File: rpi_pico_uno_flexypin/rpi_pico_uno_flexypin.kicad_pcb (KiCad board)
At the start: 2 copper layers, 68.6 x 53.3 mm, 118 parts, among them J1 Conn_01x20, J2 Conn_01x03, J3 Conn_01x20, J4 Conn_01x03, J5 Conn_SPI, J6 Conn_01x08, J7 Conn_01x06, J8 Conn_01x10, J9 Conn_01x08, SW1 SW_RST, U1 RaspberryPi_Pico

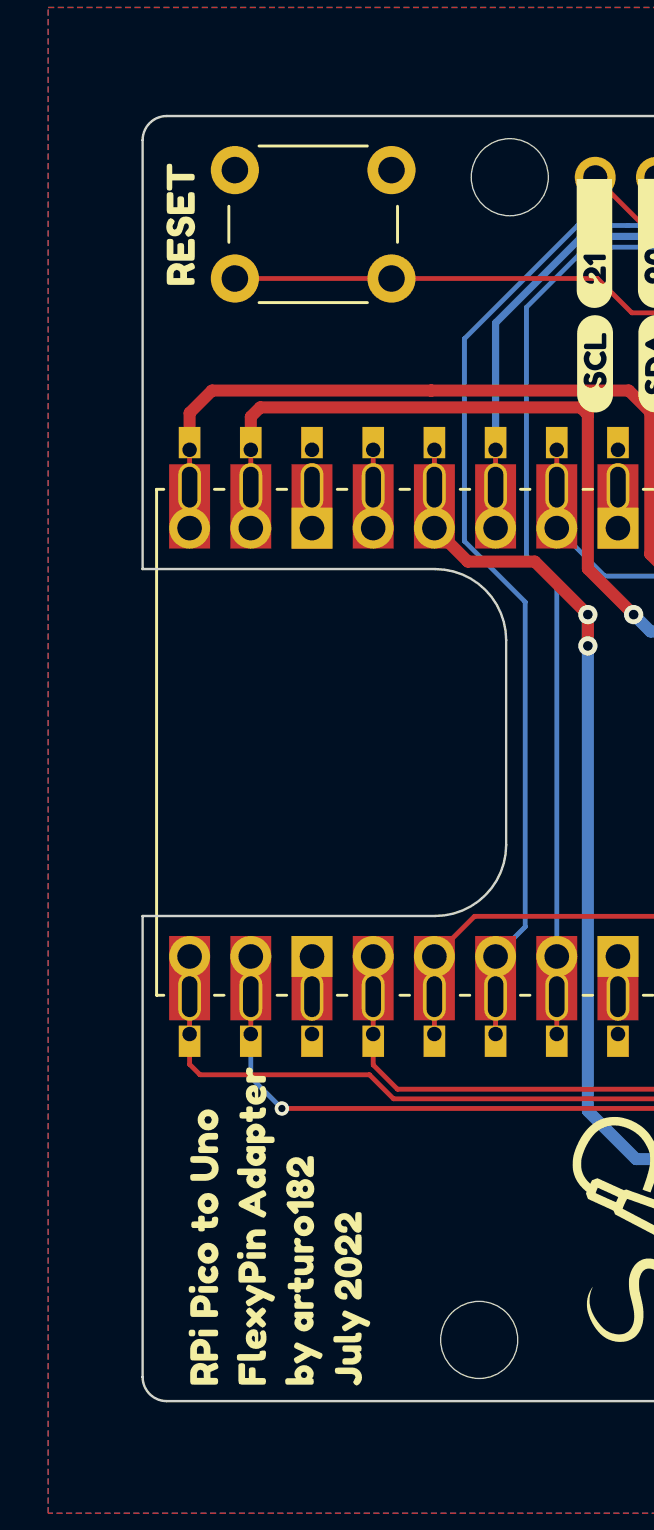
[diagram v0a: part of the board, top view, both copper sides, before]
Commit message: Change Pico Adapters' Reset Button to SMD
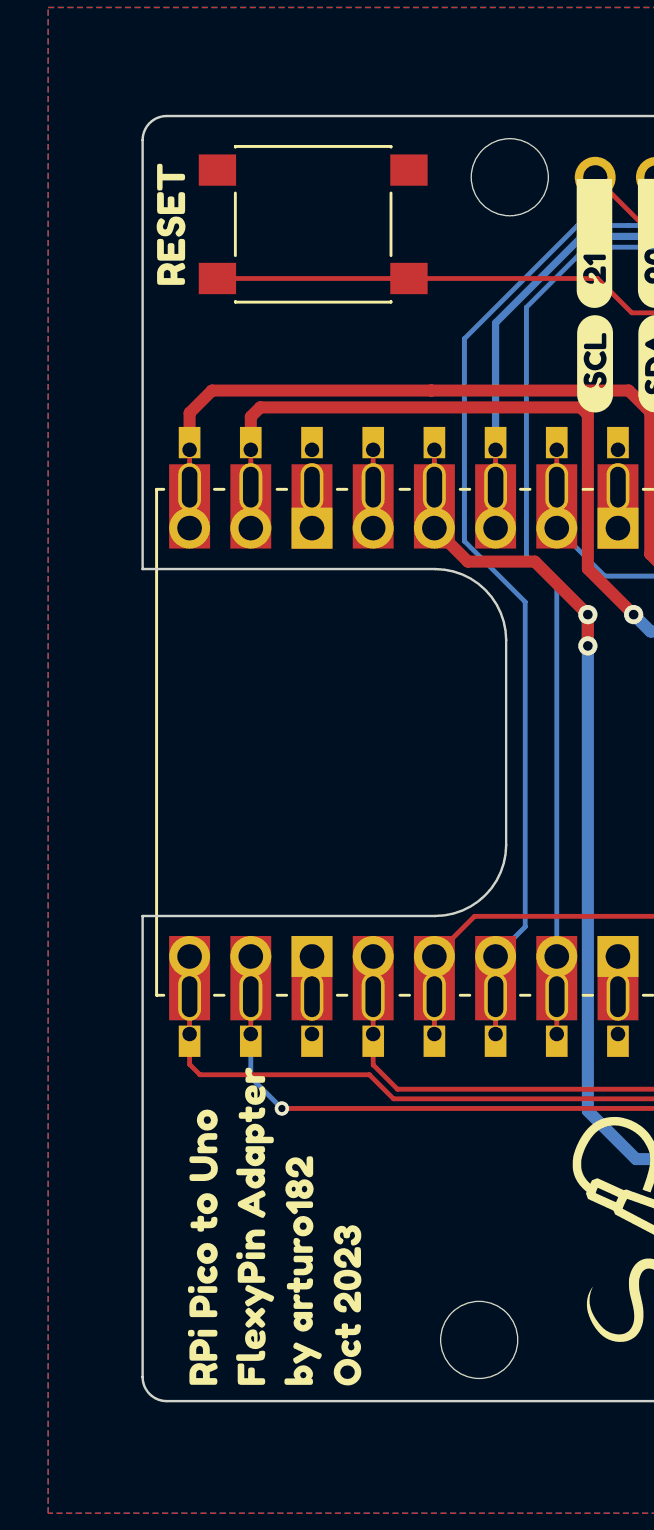
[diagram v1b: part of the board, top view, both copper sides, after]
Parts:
- removed kibuzzard-62CF07F8 (x2): G***, kibuzzard-62CF07F8
- added kibuzzard-653EF9BD: G***, kibuzzard-653EF9BD, F.Cu at (116.9, 125.6)
- added kibuzzard-653EF9BD: G***, kibuzzard-653EF9BD, B.Cu at (117.0, 125.9)
- SW1: footprint Button_Switch_THT:SW_PUSH_6mm -> Button_Switch_SMD:SW_Push_1P1T_NO_6x6mm_H9.5mm
- moved SW1 3.95 mm to (118.5, 84.0)
- moved kibuzzard-6227DBF8 0.40 mm to (112.6, 84.0)
